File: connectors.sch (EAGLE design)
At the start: 15 parts, among them CON1 PINHEAD_1X06-2, CON2 PINHEAD_1X03-2.54-RA, CON3 CON-4P-JST_GH-RA, CON4 PINHEAD_1X02-2, CON5 PINHEAD_1X02-2, CON8 CON-4P-JST_GH-RA, IC3 TJA1051

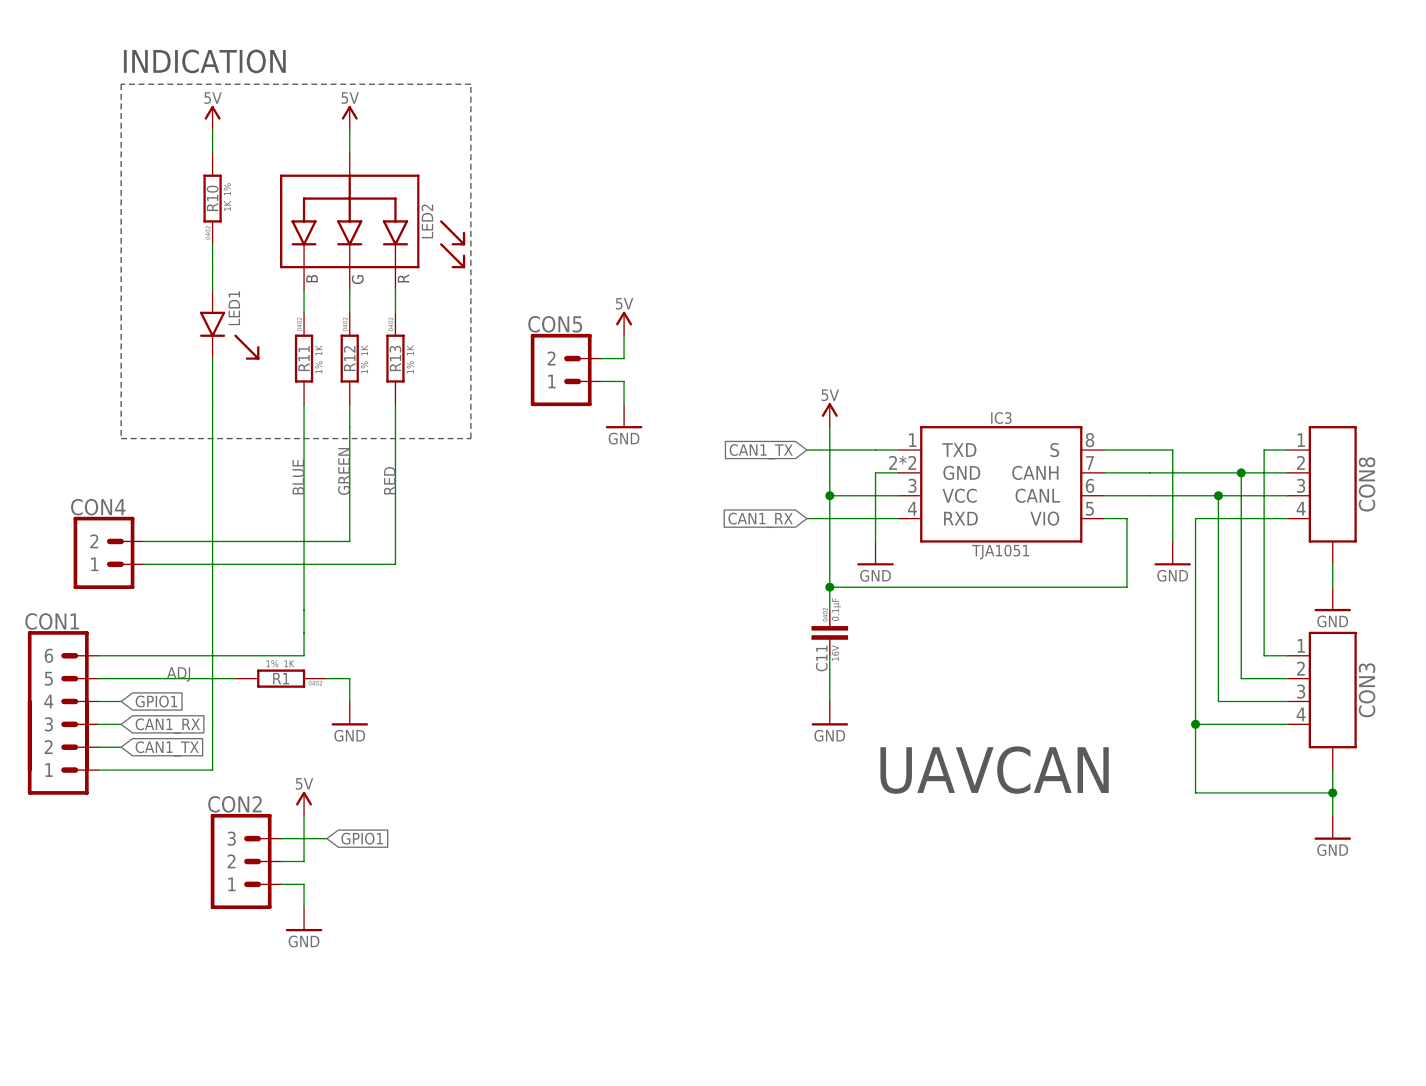
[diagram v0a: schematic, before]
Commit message: here comes UAVCAN BEC output
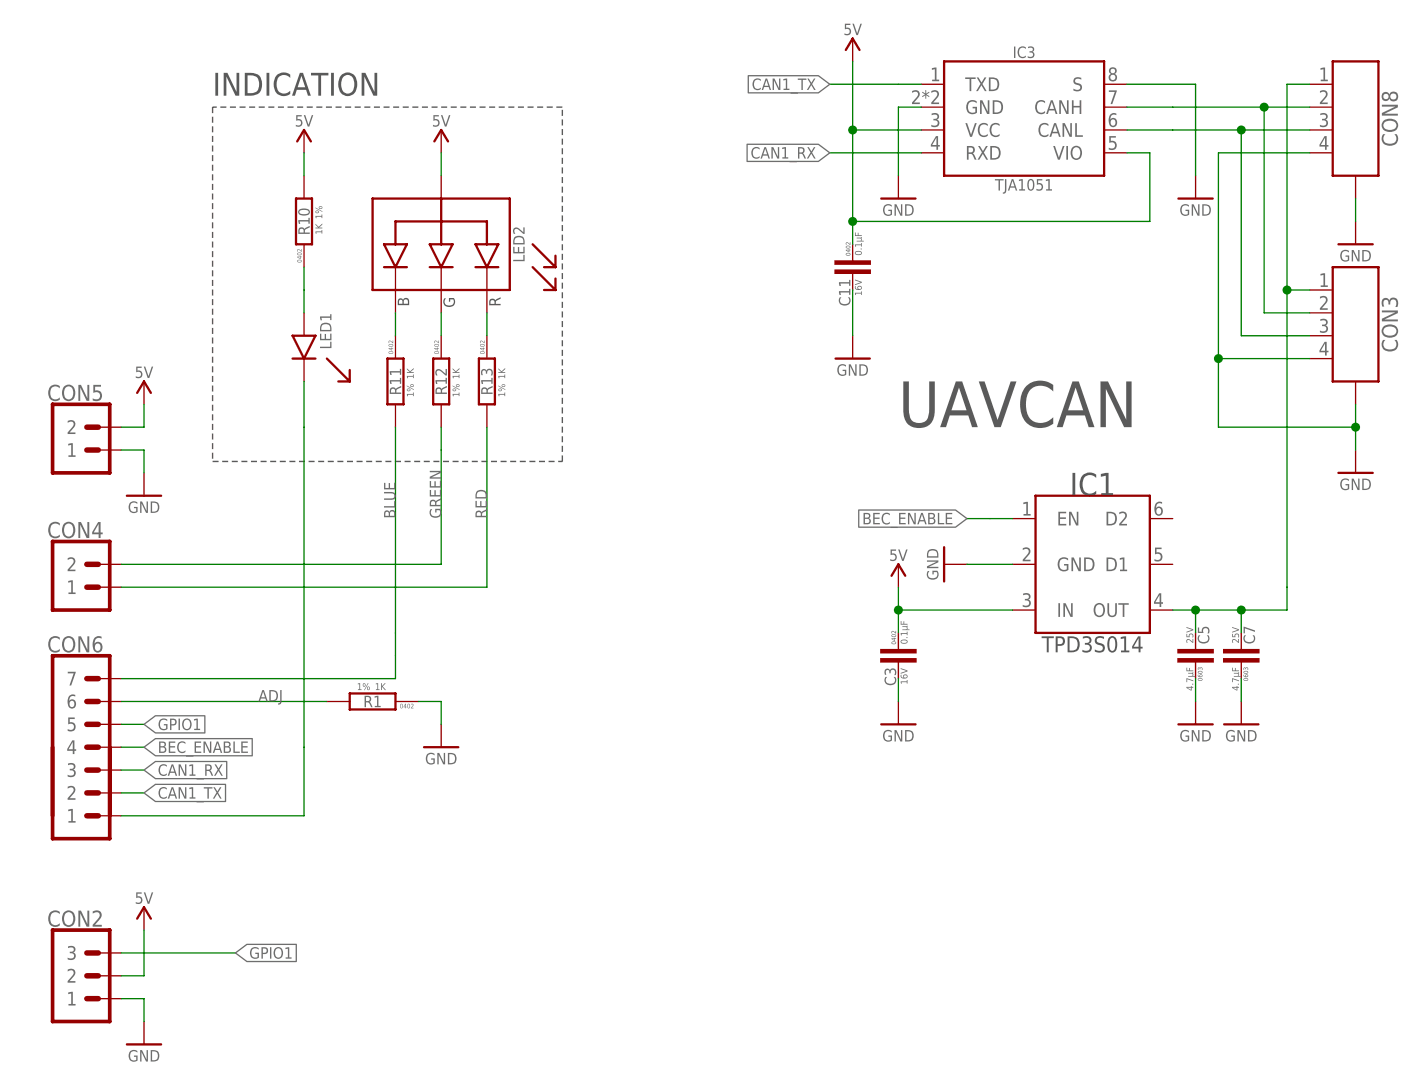
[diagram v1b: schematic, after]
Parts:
- removed CON1: PINHEAD_1X06-2, pinhead:PINHEAD_1X06-2
- added C3: 0.1µF, C_digikey:0.1µF-16V_10%_X7R-0402
- added C5, C7: 4.7µF, C_digikey:4.7µF-25V_10%_X6S-0603
- added CON6: PINHEAD_1X07-2, pinhead:PINHEAD_1X07-2
- added IC1: TPD3S014DBVR-SOT23-6, myxa_masterlib:TPD3S014DBVR-SOT23-6
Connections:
- removed net N$28: CON3.1, CON8.1
- new net BEC_ENABLE: CON6.4, IC1.EN
- new net CAN1_VDD: C5.2, C7.2, CON3.1, CON8.1, IC1.OUT
- net ADJ: now also CON6.6; no longer CON1.5
- net BLUE: now also CON6.7; no longer CON1.6
- net CAN1_LED: now also CON6.1; no longer CON1.1
- net CAN1_RX: now also CON6.3; no longer CON1.3
- net CAN1_TX: now also CON6.2; no longer CON1.2
- net GND: now also C3.2, C5.1, C7.1, IC1.GND
- net GPIO1: now also CON6.5; no longer CON1.4
- net VDD_5V: now also C3.1, IC1.IN
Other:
- moved on the sheet: C11, CON2, CON3, CON4, CON5, CON8, IC3, LED1, LED2, R1, R10, R11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
